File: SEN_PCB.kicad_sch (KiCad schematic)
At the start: 8 parts, among them J1 47080-4005, U1 BME680, U2 ADT7310

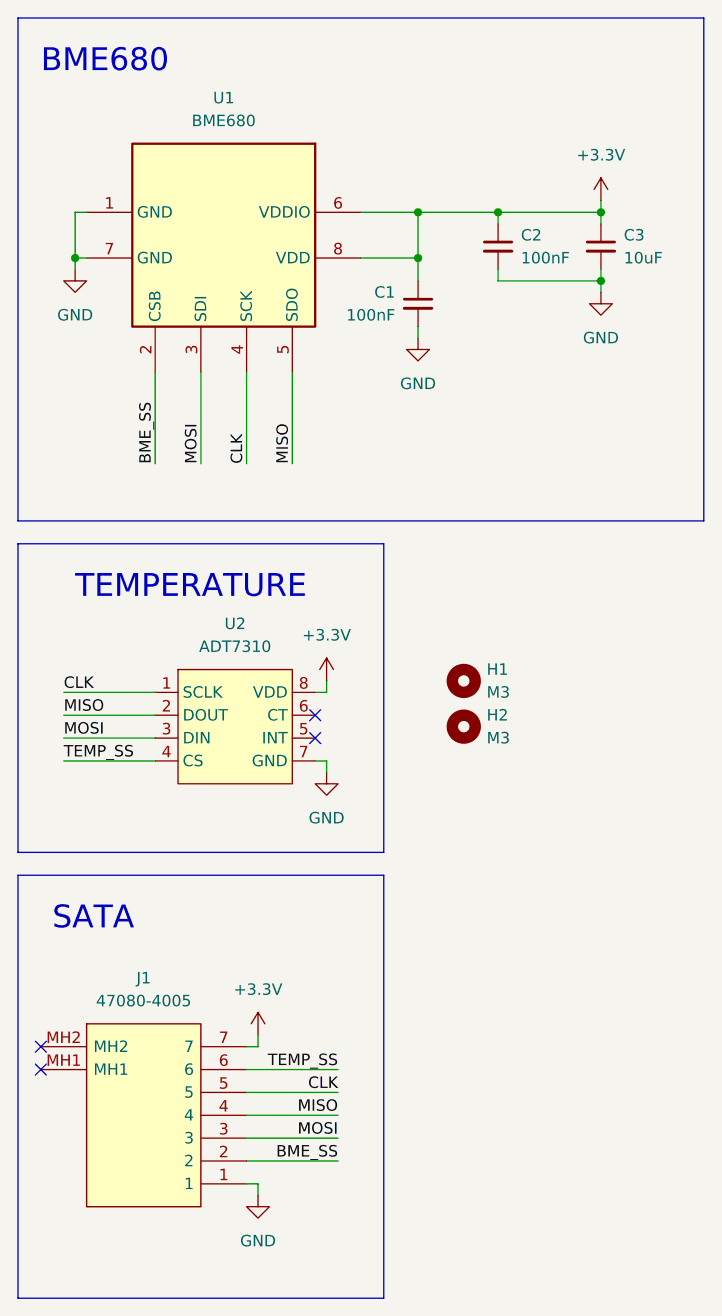
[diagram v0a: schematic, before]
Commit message: 1V KiCad
Changed form-factor to more appropriate one.
Changed connector pinout meaning to match new pinout on MCU board.
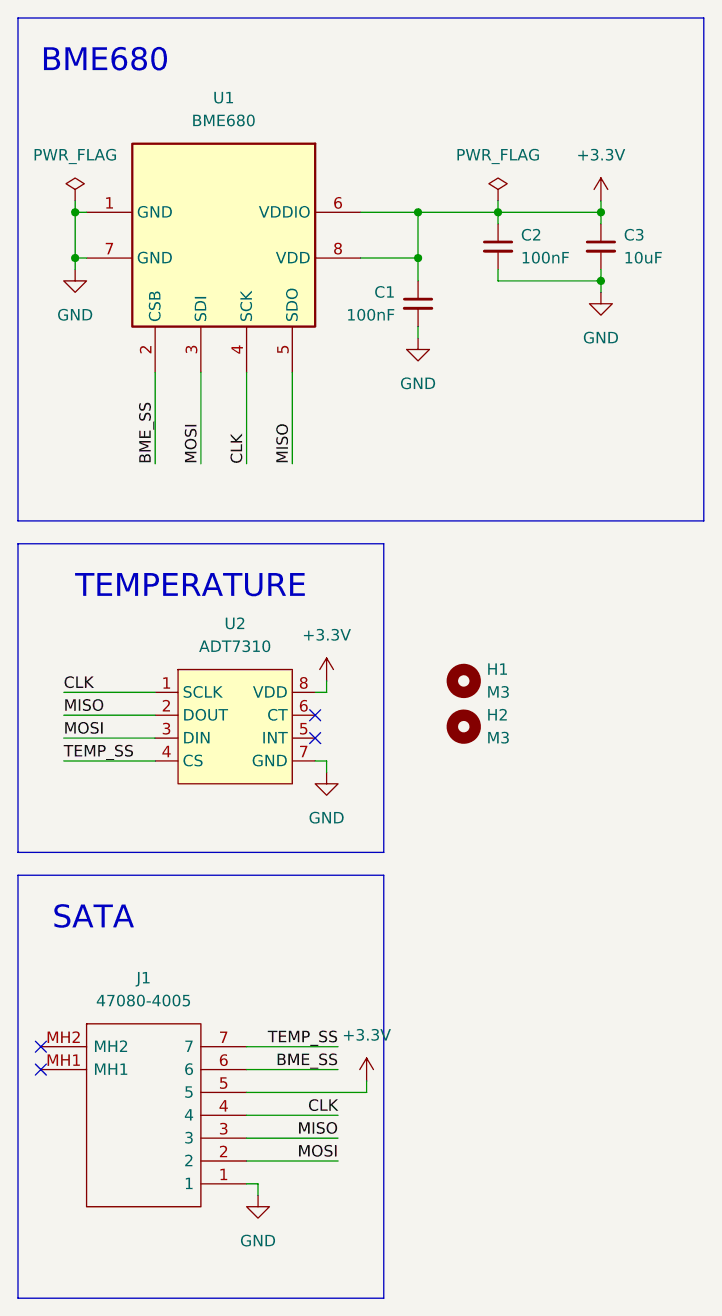
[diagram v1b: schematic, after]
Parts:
- J1: footprint LOCAL:470804005 -> 470804005
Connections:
- net +3.3V: now also J1.5; no longer J1.7
- net BME_SS: now also J1.6; no longer J1.2
- net CLK: now also J1.4; no longer J1.5
- net MISO: now also J1.3; no longer J1.4
- net MOSI: now also J1.2; no longer J1.3
- net TEMP_SS: now also J1.7; no longer J1.6
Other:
- company: (none) -> BASEMENT
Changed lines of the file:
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@@
 (kicad_sch (version 20211123) (generator eeschema)
   (paper "A4")
+  (title_block
+    (date "%%date%%")
+    (rev "%%version%%")
+    (company "BASEMENT")
+  )
   (junction (at 80.01 43.18) (diameter 0) (color 0 0 0 0)
   )
@@
   )
   (junction (at 100.33 45.72) (diameter 0) (color 0 0 0 0)
+  )
+  (junction (at 41.91 38.1) (diameter 0) (color 0 0 0 0)
   )
   (junction (at 100.33 38.1) (diameter 0) (color 0 0 0 0)
@@
     (stroke (width 0) (type default) (color 0 0 0 0))
   )
-  (wire (pts (xy 60.96 130.81) (xy 62.23 130.81))
+  (wire (pts (xy 60.96 140.97) (xy 71.12 140.97))
+    (stroke (width 0) (type default) (color 0 0 0 0))
+  )
+  (wire (pts (xy 55.88 55.88) (xy 55.88 66.04))
+    (stroke (width 0) (type default) (color 0 0 0 0))
+  )
+  (wire (pts (xy 60.96 55.88) (xy 60.96 66.04))
+    (stroke (width 0) (type default) (color 0 0 0 0))
+  )
+  (wire (pts (xy 50.8 55.88) (xy 50.8 66.04))
+    (stroke (width 0) (type default) (color 0 0 0 0))
+  )
+  (polyline (pts (xy 111.76 72.39) (xy 35.56 72.39))
+    (stroke (width 0) (type default) (color 0 0 0 0))
+  )
+  (polyline (pts (xy 35.56 74.93) (xy 76.2 74.93))
+    (stroke (width 0) (type default) (color 0 0 0 0))
+  )
+  (polyline (pts (xy 76.2 158.75) (xy 35.56 158.75))
+    (stroke (width 0) (type default) (color 0 0 0 0))
+  )
+  (wire (pts (xy 43.18 38.1) (xy 41.91 38.1))
+    (stroke (width 0) (type default) (color 0 0 0 0))
+  )
+  (wire (pts (xy 88.9 45.72) (xy 100.33 45.72))
+    (stroke (width 0) (type default) (color 0 0 0 0))
+  )
+  (wire (pts (xy 88.9 36.83) (xy 88.9 38.1))
+    (stroke (width 0) (type default) (color 0 0 0 0))
+  )
+  (wire (pts (xy 43.18 43.18) (xy 41.91 43.18))
+    (stroke (width 0) (type default) (color 0 0 0 0))
+  )
+  (wire (pts (xy 68.58 99.06) (xy 69.85 99.06))
+    (stroke (width 0) (type default) (color 0 0 0 0))
+  )
+  (wire (pts (xy 60.96 135.89) (xy 74.295 135.89))
+    (stroke (width 0) (type default) (color 0 0 0 0))
+  )
+  (wire (pts (xy 80.01 43.18) (xy 80.01 45.72))
+    (stroke (width 0) (type default) (color 0 0 0 0))
+  )
+  (polyline (pts (xy 76.2 109.22) (xy 35.56 109.22))
     (stroke (width 0) (type default) (color 0 0 0 0))
   )
@@
     (stroke (width 0) (type default) (color 0 0 0 0))
   )
-  (wire (pts (xy 55.88 55.88) (xy 55.88 66.04))
-    (stroke (width 0) (type default) (color 0 0 0 0))
-  )
-  (wire (pts (xy 60.96 55.88) (xy 60.96 66.04))
-    (stroke (width 0) (type default) (color 0 0 0 0))
-  )
-  (wire (pts (xy 50.8 55.88) (xy 50.8 66.04))
-    (stroke (width 0) (type default) (color 0 0 0 0))
-  )
-  (polyline (pts (xy 111.76 72.39) (xy 35.56 72.39))
-    (stroke (width 0) (type default) (color 0 0 0 0))
-  )
-  (polyline (pts (xy 35.56 74.93) (xy 76.2 74.93))
-    (stroke (width 0) (type default) (color 0 0 0 0))
-  )
-  (polyline (pts (xy 76.2 158.75) (xy 35.56 158.75))
-    (stroke (width 0) (type default) (color 0 0 0 0))
-  )
-  (wire (pts (xy 43.18 38.1) (xy 41.91 38.1))
-    (stroke (width 0) (type default) (color 0 0 0 0))
-  )
-  (wire (pts (xy 88.9 45.72) (xy 100.33 45.72))
-    (stroke (width 0) (type default) (color 0 0 0 0))
-  )
-  (wire (pts (xy 43.18 43.18) (xy 41.91 43.18))
-    (stroke (width 0) (type default) (color 0 0 0 0))
-  )
-  (wire (pts (xy 68.58 99.06) (xy 69.85 99.06))
-    (stroke (width 0) (type default) (color 0 0 0 0))
-  )
-  (wire (pts (xy 80.01 43.18) (xy 80.01 45.72))
-    (stroke (width 0) (type default) (color 0 0 0 0))
-  )
-  (polyline (pts (xy 76.2 109.22) (xy 35.56 109.22))
-    (stroke (width 0) (type default) (color 0 0 0 0))
-  )
-  (wire (pts (xy 60.96 135.89) (xy 71.12 135.89))
-    (stroke (width 0) (type default) (color 0 0 0 0))
-  )
   (wire (pts (xy 73.66 38.1) (xy 80.01 38.1))
     (stroke (width 0) (type default) (color 0 0 0 0))
   )
+  (wire (pts (xy 60.96 133.35) (xy 71.12 133.35))
+    (stroke (width 0) (type default) (color 0 0 0 0))
+  )
+  (polyline (pts (xy 35.56 111.76) (xy 35.56 158.75))
+    (stroke (width 0) (type default) (color 0 0 0 0))
+  )
   (wire (pts (xy 60.96 143.51) (xy 71.12 143.51))
     (stroke (width 0) (type default) (color 0 0 0 0))
   )
-  (polyline (pts (xy 35.56 111.76) (xy 35.56 158.75))
-    (stroke (width 0) (type default) (color 0 0 0 0))
-  )
-  (wire (pts (xy 60.96 140.97) (xy 71.12 140.97))
-    (stroke (width 0) (type default) (color 0 0 0 0))
-  )
-  (wire (pts (xy 62.23 130.81) (xy 62.23 129.54))
+  (wire (pts (xy 74.295 135.89) (xy 74.295 134.62))
     (stroke (width 0) (type default) (color 0 0 0 0))
   )
@@
     (stroke (width 0) (type default) (color 0 0 0 0))
   )
-  (wire (pts (xy 60.96 133.35) (xy 71.12 133.35))
+  (wire (pts (xy 60.96 130.81) (xy 71.12 130.81))
     (stroke (width 0) (type default) (color 0 0 0 0))
   )
@@
   )
   (wire (pts (xy 80.01 38.1) (xy 88.9 38.1))
+    (stroke (width 0) (type default) (color 0 0 0 0))
+  )
+  (wire (pts (xy 41.91 36.83) (xy 41.91 38.1))
     (stroke (width 0) (type default) (color 0 0 0 0))
   )
@@
     (effects (font (size 1.27 1.27)) (justify left bottom))
   )
-  (label "BME_SS" (at 71.12 143.51 180)
+  (label "BME_SS" (at 71.12 133.35 180)
     (effects (font (size 1.27 1.27)) (justify right bottom))
   )
@@
     (effects (font (size 1.27 1.27)) (justify left bottom))
   )
-  (label "CLK" (at 71.12 135.89 180)
+  (label "CLK" (at 71.12 138.43 180)
     (effects (font (size 1.27 1.27)) (justify right bottom))
   )
-  (label "MISO" (at 71.12 138.43 180)
+  (label "MISO" (at 71.12 140.97 180)
     (effects (font (size 1.27 1.27)) (justify right bottom))
   )
-  (label "TEMP_SS" (at 71.12 133.35 180)
+  (label "TEMP_SS" (at 71.12 130.81 180)
     (effects (font (size 1.27 1.27)) (justify right bottom))
   )
@@
     (effects (font (size 1.27 1.27)) (justify left bottom))
   )
-  (label "MOSI" (at 71.12 140.97 180)
+  (label "MOSI" (at 71.12 143.51 180)
     (effects (font (size 1.27 1.27)) (justify right bottom))
   )
@@
     (property "Reference" "J1" (id 0) (at 49.53 123.19 0))
     (property "Value" "47080-4005" (id 1) (at 49.53 125.73 0))
-    (property "Footprint" "LOCAL:470804005" (id 2) (at 57.15 128.27 0)
+    (property "Footprint" "470804005" (id 2) (at 57.15 128.27 0)
       (effects (font (size 1.27 1.27)) (justify left) hide)
     )
@@
     )
   )
-  (symbol (lib_id "power:+3.3V") (at 62.23 129.54 0) (unit 1)
-    (in_bom yes) (on_board yes) (fields_autoplaced)
-    (property "Reference" "#PWR0108" (id 0) (at 62.23 133.35 0)
-      (effects (font (size 1.27 1.27)) hide)
-    )
-    (property "Value" "+3.3V" (id 1) (at 62.23 124.46 0))
-    (property "Footprint" "" (id 2) (at 62.23 129.54 0)
-      (effects (font (size 1.27 1.27)) hide)
-    )
-    (property "Datasheet" "" (id 3) (at 62.23 129.54 0)
+  (symbol (lib_id "power:PWR_FLAG") (at 41.91 36.83 0) (unit 1)
+    (in_bom yes) (on_board yes) (fields_autoplaced)
+    (property "Reference" "#FLG0102" (id 0) (at 41.91 34.925 0)
+      (effects (font (size 1.27 1.27)) hide)
+    )
+    (property "Value" "PWR_FLAG" (id 1) (at 41.91 31.75 0))
+    (property "Footprint" "" (id 2) (at 41.91 36.83 0)
+      (effects (font (size 1.27 1.27)) hide)
+    )
+    (property "Datasheet" "~" (id 3) (at 41.91 36.83 0)
+      (effects (font (size 1.27 1.27)) hide)
+    )
+    (pin "1")
+  )
+  (symbol (lib_id "power:+3.3V") (at 74.295 134.62 0) (unit 1)
+    (in_bom yes) (on_board yes) (fields_autoplaced)
+    (property "Reference" "#PWR0108" (id 0) (at 74.295 138.43 0)
+      (effects (font (size 1.27 1.27)) hide)
+    )
+    (property "Value" "+3.3V" (id 1) (at 74.295 129.54 0))
+    (property "Footprint" "" (id 2) (at 74.295 134.62 0)
+      (effects (font (size 1.27 1.27)) hide)
+    )
+    (property "Datasheet" "" (id 3) (at 74.295 134.62 0)
+      (effects (font (size 1.27 1.27)) hide)
+    )
+    (pin "1")
+  )
+  (symbol (lib_id "power:PWR_FLAG") (at 88.9 36.83 0) (unit 1)
+    (in_bom yes) (on_board yes) (fields_autoplaced)
+    (property "Reference" "#FLG0101" (id 0) (at 88.9 34.925 0)
+      (effects (font (size 1.27 1.27)) hide)
+    )
+    (property "Value" "PWR_FLAG" (id 1) (at 88.9 31.75 0))
+    (property "Footprint" "" (id 2) (at 88.9 36.83 0)
+      (effects (font (size 1.27 1.27)) hide)
+    )
+    (property "Datasheet" "~" (id 3) (at 88.9 36.83 0)
       (effects (font (size 1.27 1.27)) hide)
     )
@@
   )
   (symbol_instances
+    (path "/b68df7da-69a1-490b-8a20-dfe9b96c653e"
+      (reference "#FLG0101") (unit 1) (value "PWR_FLAG") (footprint "")
+    )
+    (path "/8f524464-4d08-48b3-9f91-9f42531496b5"
+      (reference "#FLG0102") (unit 1) (value "PWR_FLAG") (footprint "")
+    )
     (path "/fd5a6141-96ae-4b63-a240-0e41eba98fe5"
       (reference "#PWR0101") (unit 1) (value "+3.3V") (footprint "")
@@
     )
     (path "/092e7aed-35d7-4419-82ac-1a819a463ca8"
-      (reference "J1") (unit 1) (value "47080-4005") (footprint "LOCAL:470804005")
+      (reference "J1") (unit 1) (value "47080-4005") (footprint "470804005")
     )
     (path "/02d25d9f-ce5f-4fda-8a28-4eaa842e613b"
